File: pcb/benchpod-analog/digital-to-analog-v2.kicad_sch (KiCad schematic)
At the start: 70 parts, among them J9 Screw_Terminal_01x02, K1 G6K-2F-Y DC5, K2 G6K-2F-Y DC5, Q1 BCP56, U12 HX PZ2.54-1X2P ZZ, U13 HX PZ2.54-1X2P ZZ, U14 HX PZ2.54-1X2P ZZ, U43 DAC8554IPWR, U44 OPA2365AIDR, U45 OPA2992IDR, U51 OPA2992IDR, U9 XTR116UA/2K5

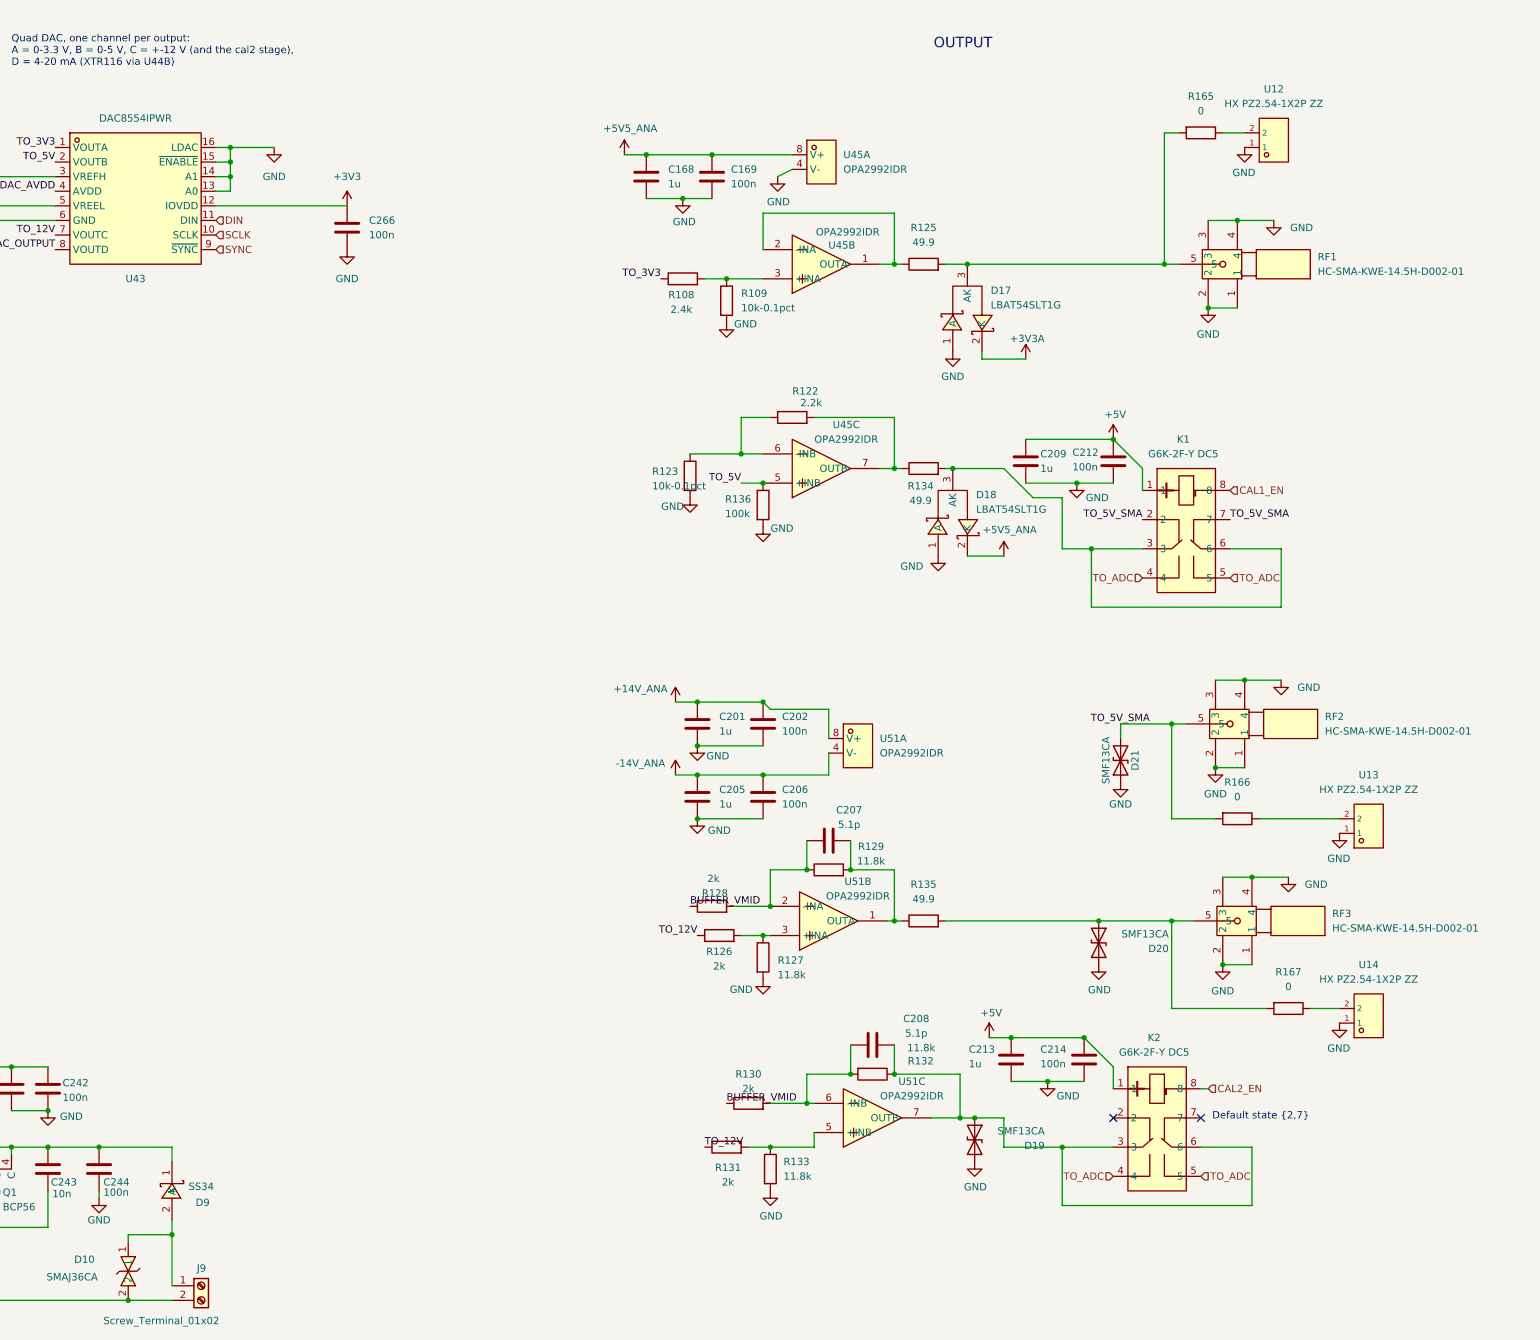
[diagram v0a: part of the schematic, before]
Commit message: analog only board: enclosure connectors (BNC, pluggable 4-20 mA blocks)
Per benchpod-private enclosure/design.md:
- RF2 (0-5 V), RF3 (+-12 V), RF4 (ADC in): SMA -> right-angle BNC
  KH-BNC50-3511 (C2837587). Center on the same net, shell + lugs to GND.
- RF1 (0-3.3 V jack) removed; the 0-3.3 V output stays on TP1.
- 2-pin test headers U11-U14 and their 0 ohm links R20, R165-R167 removed;
  test pads TP1-TP4 (1.5 mm, not in the BOM) on the four outputs instead.
- J8 (4-20 mA in) and J9 (4-20 mA out): 5.08 mm screw terminals ->
  3.81 mm right-angle pluggable WJ15EDGRC-3.81-02P (C8387, green); the
  mating plug C8466 is bought separately.

Co-Authored-By: Claude Opus 5.5 <noreply@anthropic.com>
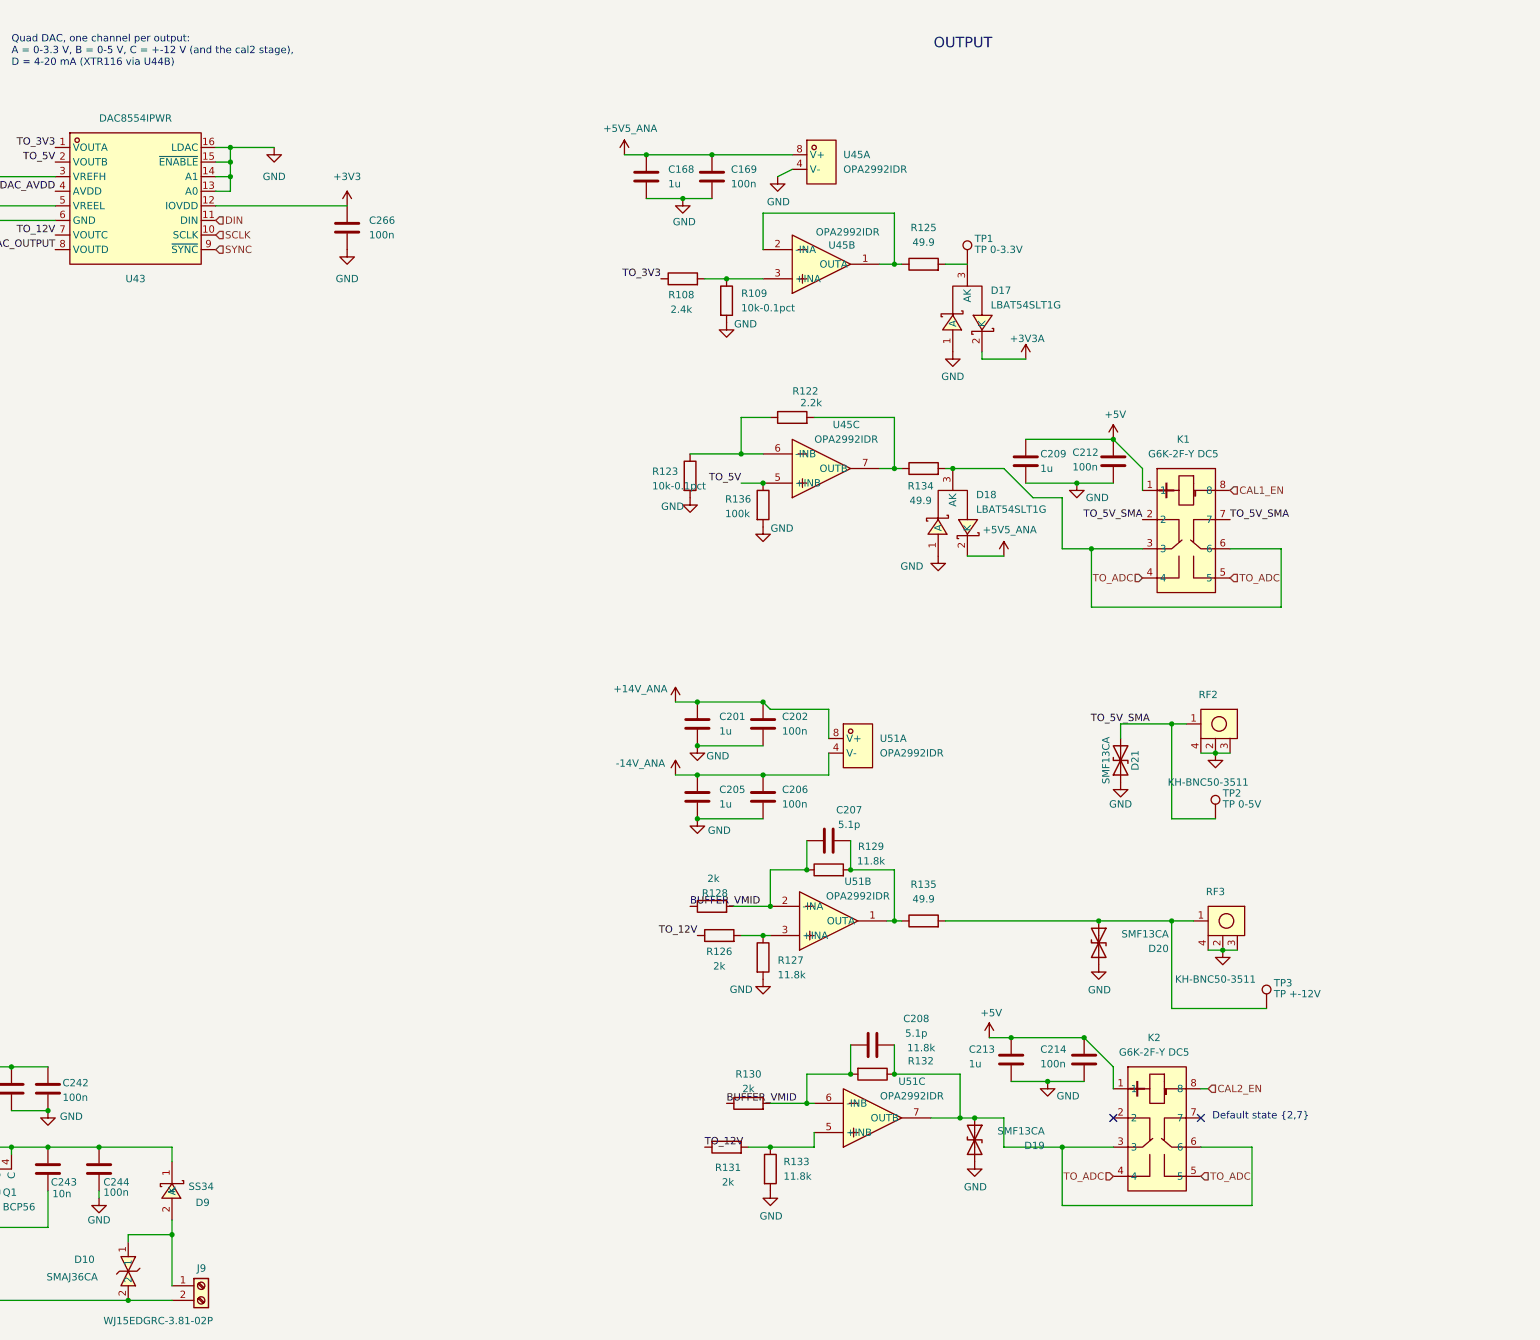
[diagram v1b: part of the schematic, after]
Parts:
- removed R165, R166, R167: 0, Resistor_SMD:R_0402_1005Metric, symbol Device:R
- removed RF1, RF2, RF3: HC-SMA-KWE-14.5H-D002-01, lcsc:SMA-TH_BWSMA-KWE-Z001, symbol lcsc_lib:BWSMA-KWE-Z001
- removed U12, U13, U14: HX PZ2.54-1X2P ZZ, lcsc_footprints:C32713268_HDR-TH_2P-P2_54-V-M-3, symbol lcsc_plugin:HX_PZ2_54-1X2P_ZZ
- added RF2, RF3: KH-BNC50-3511, lcsc_footprints:C2837587_ANT-TH_KH-BNC50-3511, symbol lcsc_imported:KH-BNC50-3511_C2837587
- added TP1: TP 0-3.3V, TestPoint:TestPoint_Pad_D1.5mm, symbol Connector:TestPoint
- added TP2: TP 0-5V, TestPoint:TestPoint_Pad_D1.5mm, symbol Connector:TestPoint
- added TP3: TP +-12V, TestPoint:TestPoint_Pad_D1.5mm, symbol Connector:TestPoint
- J9: value Screw_Terminal_01x02 -> WJ15EDGRC-3.81-02P; footprint lcsc:CONN-TH_2P-P5.00_WJ500V-5.08-2P -> lcsc_footprints:C8387_CONN-TH_2P-P3.81_WJ15EDGRC-3.81-2P; LCSC C8465 -> C8387
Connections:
- net GND: now also RF2.2 (GND), RF2.3 (MNT), RF2.4 (MNT), RF3.2 (GND), RF3.3 (MNT), RF3.4 (MNT)
- net TO_5V_SMA: now also RF2.1 (OUT), TP2.1
- net at D17.3 (AK), R125.2: now also TP1.1
- net at D20.1 (A1), R135.2: now also RF3.1 (OUT), TP3.1

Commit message: analog only board: DAC outputs on one 6-pin pluggable block
RF2 (0-5 V) and RF3 (+-12 V) BNCs removed. All three DAC outputs go to
J11, a 3.81 mm right-angle pluggable block WJ15EDGRC-3.81-06P (C7246,
green): 1 0-3.3 V (OUT_3V3), 2 GND, 3 0-5 V (TO_5V_SMA), 4 GND,
5 +-12 V (OUT_12V), 6 GND. The 0-3.3 V output is on the panel again.
TP1-TP3 stay as internal test pads. Panel: 1 BNC (ADC in), the 6-pin DAC
block, and the two 2-pin 4-20 mA blocks.

Co-Authored-By: Claude Opus 5.5 <noreply@anthropic.com>
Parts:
- removed RF2, RF3: KH-BNC50-3511, lcsc_footprints:C2837587_ANT-TH_KH-BNC50-3511, symbol lcsc_imported:KH-BNC50-3511_C2837587
- added J11: WJ15EDGRC-3.81-06P, lcsc_footprints:C7246_CONN-TH_WJ15EDGRC-3.81-6P, symbol Connector:Screw_Terminal_01x06
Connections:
- net GND: now also J11.2 (Pin_2), J11.4 (Pin_4), J11.6 (Pin_6)
- net TO_5V_SMA: now also J11.3 (Pin_3)
- net OUT_12V: now reaches D20.1 (A1), R135.2, TP3.1
- net OUT_12V: now also J11.5 (Pin_5)
- net OUT_3V3: now reaches D17.3 (AK), R125.2, TP1.1
- net OUT_3V3: now also J11.1 (Pin_1)
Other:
- note added: "J11: DAC outputs on one 6-pin pluggable block (0-3.3 V, 0-5 V, +-12 V, each with its own GND). The ADC input keeps the BNC (J10 on the ADC sheet). TP1-TP3 stay as internal test pads."
